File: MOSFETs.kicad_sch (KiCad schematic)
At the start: 13 parts, among them Q1 IRF3205, Q2 IRF3205, Q3 IRF3205, Q4 IRF3205, Q5 IRF3205, Q6 IRF3205

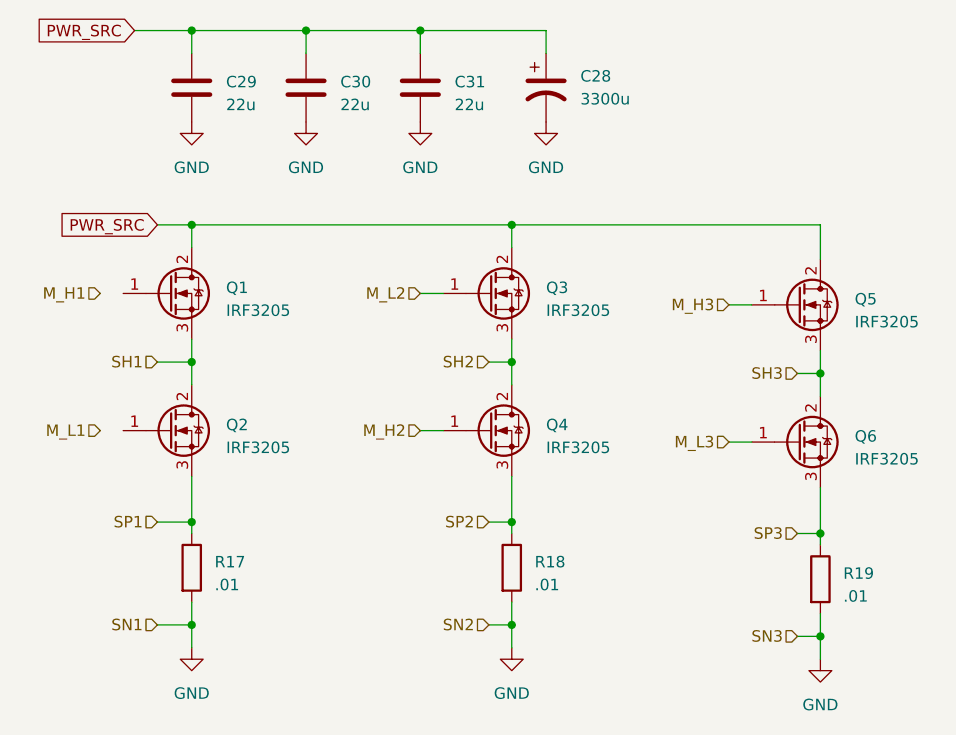
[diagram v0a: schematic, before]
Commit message: Re-annotate all components
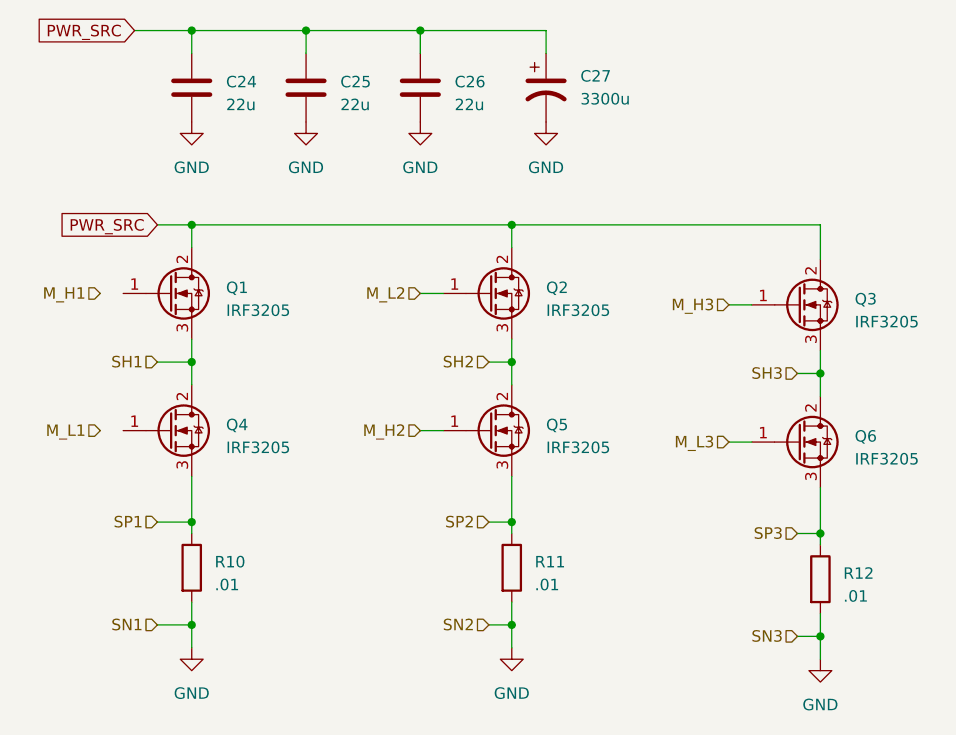
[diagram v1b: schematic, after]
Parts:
- renumbered C29 to C24, C30 to C25, C31 to C26, C28 to C27, Q3 to Q2, Q5 to Q3, Q2 to Q4, Q4 to Q5, R17 to R10, R18 to R11, R19 to R12
